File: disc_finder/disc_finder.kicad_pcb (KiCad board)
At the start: 2 copper layers, 26.5 x 21.1 mm, 12 parts, among them J1 Battery, Q1 DMN6140L-7, U1 ICM7555xB

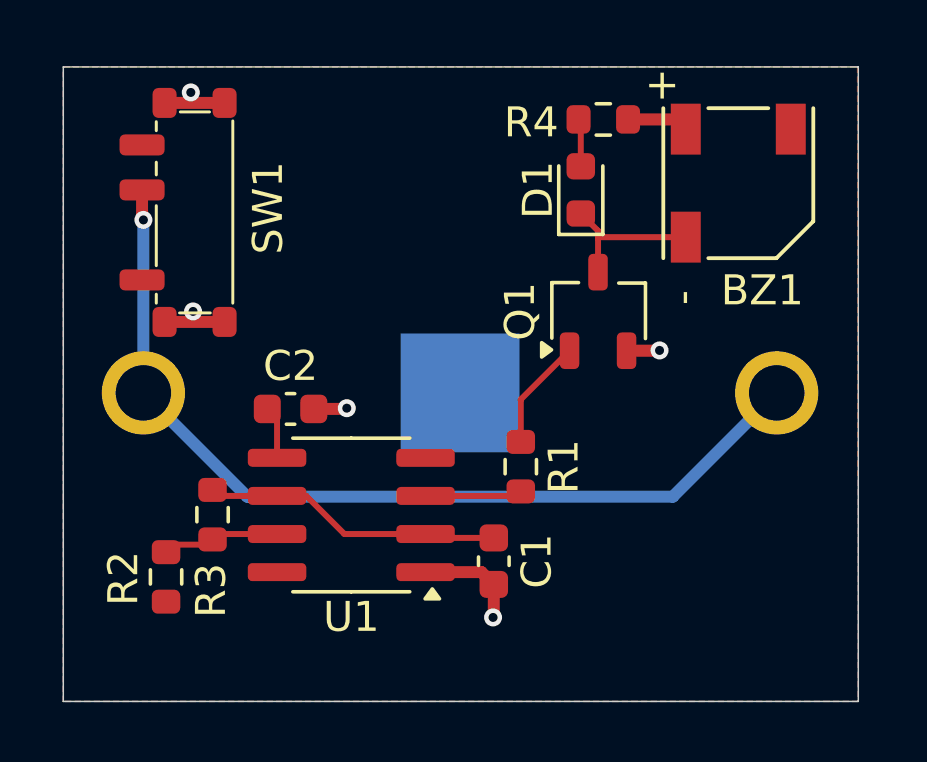
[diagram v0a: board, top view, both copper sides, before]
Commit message: Increased 555 timer frequency so that buzzer is audible, and delayed initial operation using RC
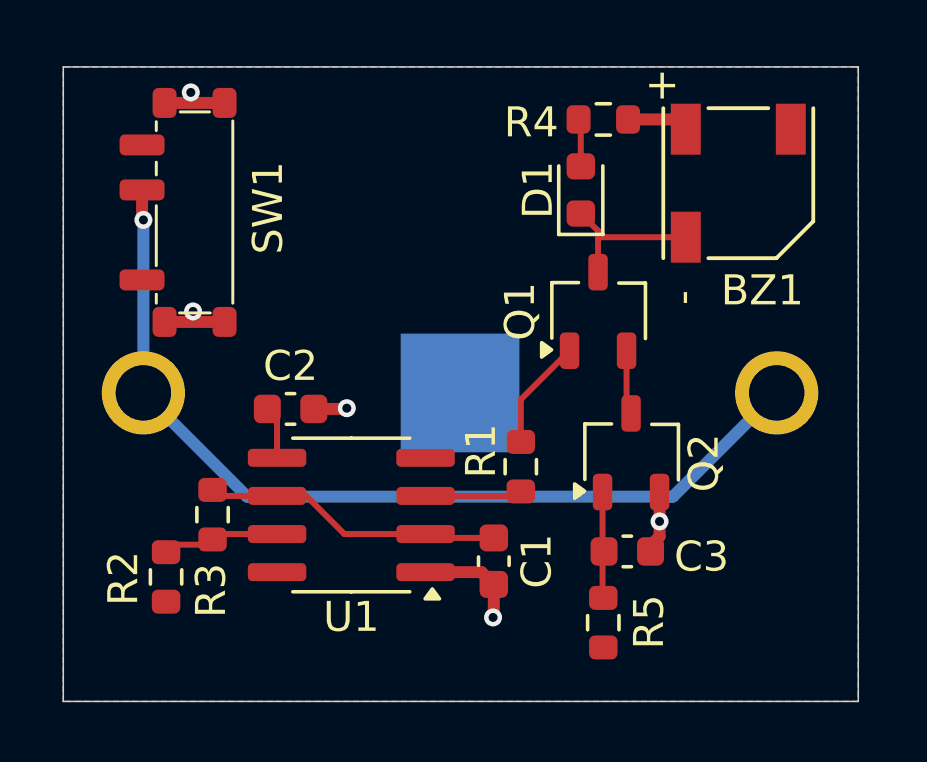
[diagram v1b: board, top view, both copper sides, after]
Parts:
- added C3: 10u, Capacitor_SMD:C_0603_1608Metric, F.Cu at (149.3, 105.0)
- added Q2: DMN6140L-7, Package_TO_SOT_SMD:TSOT-23, F.Cu at (149.4, 101.8)
- added R5: 10M, Resistor_SMD:R_0603_1608Metric, F.Cu at (148.5, 107.4)
- C1: value 1u -> 0.1u
- R3: value 1M -> 1k
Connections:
- Q1 pad 2: GND -> Net-(Q1-S)
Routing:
- net Net-(Q2-G): track 0.00 -> 3.54 mm
- net Net-(Q1-S): track 0.00 -> 2.15 mm
- net GND: track 9.77 -> 10.6 mm

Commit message: Now using a bright orange LED, and moved it to the middle of the board
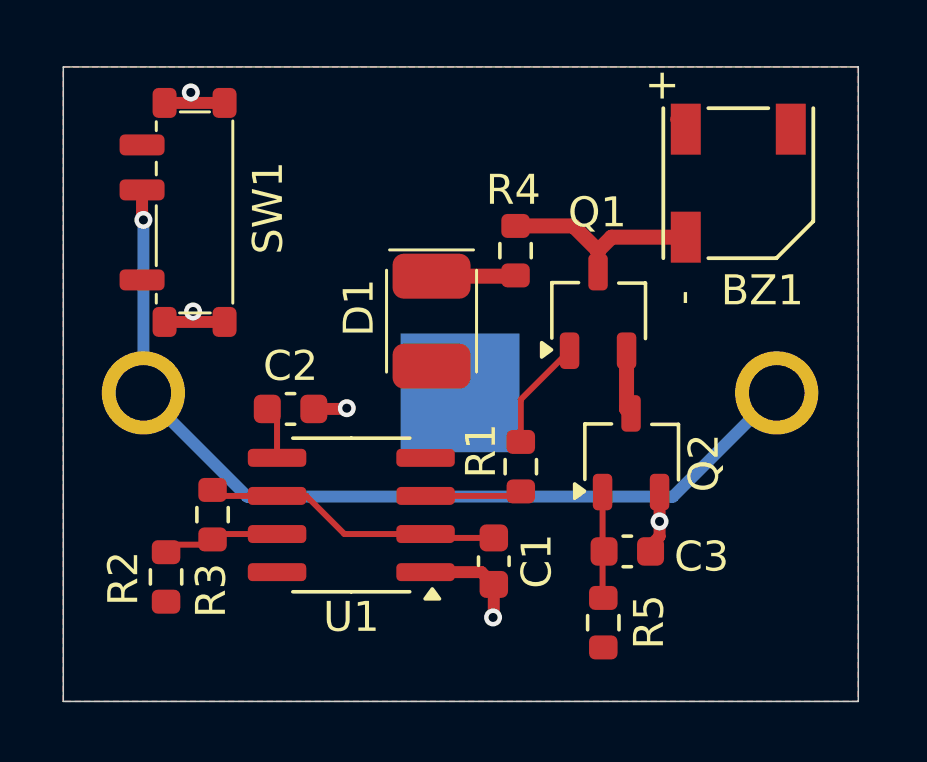
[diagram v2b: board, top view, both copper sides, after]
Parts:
- D1: footprint LED_SMD:LED_0603_1608Metric -> disc:LED_OSRAM_TOPLED
- moved D1 6.63 mm to (142.8, 97.4), turned to 0 degrees
- moved R4 5.26 mm to (145.6, 95.0), turned to 90 degrees
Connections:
- D1 pad 1: Net-(BZ1--) -> Net-(D1-K)
- D1 pad 2: Net-(D1-A) -> VDD
- R4 pad 1: VDD -> Net-(D1-K)
- R4 pad 2: Net-(D1-A) -> Net-(BZ1--)
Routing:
- net Net-(D1-K): track 0.00 -> 3.19 mm
- net Net-(BZ1--): track 5.14 -> 6.92 mm
- net VDD: track 2.06 -> 0.46 mm
- net Net-(D1-A): track 1.59 -> 0.00 mm

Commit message: Added an additional 555 timer for the led
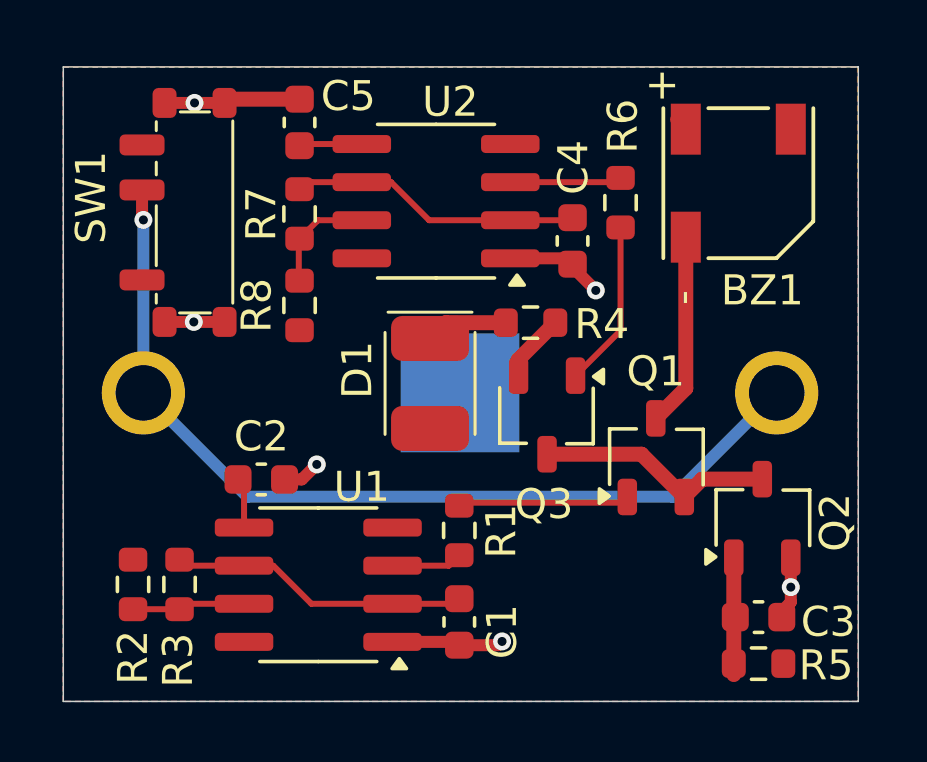
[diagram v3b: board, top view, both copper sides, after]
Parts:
- added C4: 10u, Capacitor_SMD:C_0603_1608Metric, F.Cu at (147.5, 94.7)
- added C5: 10n, Capacitor_SMD:C_0603_1608Metric, F.Cu at (138.4, 90.8)
- added Q3: DMN6140L-7, Package_TO_SOT_SMD:TSOT-23, F.Cu at (146.6, 100.5)
- added R6: 10k, Resistor_SMD:R_0603_1608Metric, F.Cu at (149.1, 93.4)
- added R7: 100k, Resistor_SMD:R_0603_1608Metric, F.Cu at (138.4, 93.8)
- added R8: 0R, Resistor_SMD:R_0603_1608Metric, F.Cu at (138.4, 96.8)
- added U2: ICM7555xB, Package_SO:SOIC-8_3.9x4.9mm_P1.27mm, F.Cu at (142.9, 93.4)
- R4: value 330R -> 100R
- moved R5 5.35 mm to (153.7, 108.8), turned to 180 degrees
- moved Q1 5.24 mm to (150.2, 101.9)
- moved C3 4.89 mm to (153.7, 107.2)
- moved Q2 4.89 mm to (153.8, 104.0)
- moved R1 2.95 mm to (143.7, 104.3)
- moved R3 2.57 mm to (134.4, 106.2)
- moved U1 2.57 mm to (139.0, 106.2)
- moved C2 2.54 mm to (137.1, 102.7)
- moved R4 2.45 mm to (146.1, 97.4), turned to 0 degrees
- moved C1 2.33 mm to (143.7, 107.4)
- moved D1 2.08 mm to (142.7, 99.5)
- moved R2 1.13 mm to (132.8, 106.2), turned to -90 degrees
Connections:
- net /555_OUT renamed /BZR_TMR_OUT
- net /TR renamed /TR_B
- R4 pad 2: Net-(BZ1--) -> Net-(Q3-S)
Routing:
- net /TR: track 0.00 -> 9.76 mm
- net GND: track 10.6 -> 16.8 mm, vias 5 -> 6
- net Net-(Q1-S): track 2.15 -> 8.01 mm
- net /LED_TMR_OUT: track 0.00 -> 5.56 mm
- net Net-(U2-Q): track 0.00 -> 3.73 mm
- net Net-(U2-DIS): track 0.00 -> 3.44 mm
- net Net-(Q3-S): track 0.00 -> 2.27 mm
- net Net-(U2-CV): track 0.00 -> 2.23 mm
- net /BZR_TMR_OUT: track 3.71 -> 5.72 mm
- net Net-(U1-Q): track 3.24 -> 2.37 mm

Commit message: Added a logo, name and revision to PCB
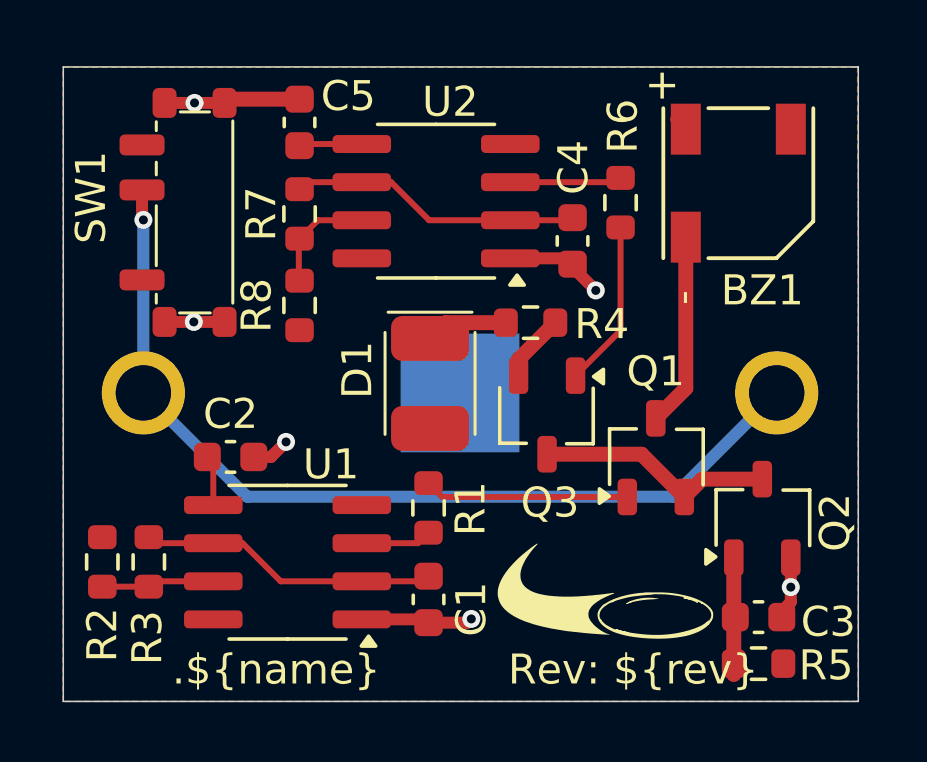
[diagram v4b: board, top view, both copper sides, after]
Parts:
- moved C2 1.27 mm to (136.1, 101.9)
- moved R3 1.27 mm to (133.4, 105.4)
- moved U1 1.27 mm to (138.0, 105.4)
- moved C1 1.27 mm to (142.7, 106.7)
- moved R1 1.27 mm to (142.7, 103.6)
- moved R2 1.27 mm to (131.8, 105.4)
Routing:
- net /BZR_TMR_OUT: track 5.72 -> 7.08 mm
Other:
- board text added: ".${name}"
- board text added: "Rev: ${rev}"
